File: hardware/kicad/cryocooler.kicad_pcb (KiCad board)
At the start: 4 copper layers, 100 x 62 mm, 330 parts, among them J1 USB_C, J10 RTD PT1000 4-wire, J11 AMP OUT (+ / -), J12 CRYOCOOLER (+ / -), J13 COMPRESSOR RELAY / GND, J14 IMU LSM6DSOX module, J2 12V IN, J3 FAN (4-pin PWM), J4 PUMP (4-pin PWM), J5 ALPHACOOL ES FLOW (3-pin), J6 ALPHACOOL ES NTC 10k, J7 PANEL BUTTON, J8 AMP REM / GND, J9 AMP SIGNAL IN / GND, Q1 IRF4905S, Q10 BSS138, Q11 BSS138, Q12 BSS138, Q2 BSS138, Q3 BSS138, Q4 BSS138, Q5 BSS138, Q6 BSS84, Q7 BSS138, Q8 BSS84, Q9 BSS138, SW1 RESET, SW2 BOOT, SW3 POWER, U1 ESP32-S3-WROOM-2-N32R16V, U10 EMC2303-x-KP, U11 LTC2954CTS8-2, U12 LM4040DBZ-5, U13 CL25N8-G, U14 ADS1220IPW, U15 AP63205WU-7, U16 LD1117S33TR, U17 ISO7741DW, U18 ACS37800KMACTR-030B3-SPI, U2 USBLC6-2SC6, U20 ADP5071AREZ, U21 LT3097ADJC, U23 INA239AIDGSR, U24 74AHCT1G125, U25 SC18IS604PW, U26 74LVC1G125, U3 SG-8002CA-PH 25MHz, U4 AD9833BRMZ, U5 OPA1656ID, U6 AD633JRZ-R7, U7 MCP4921-E/SN, U8 LM4040DBZ-2.5, U9 OPA188ID

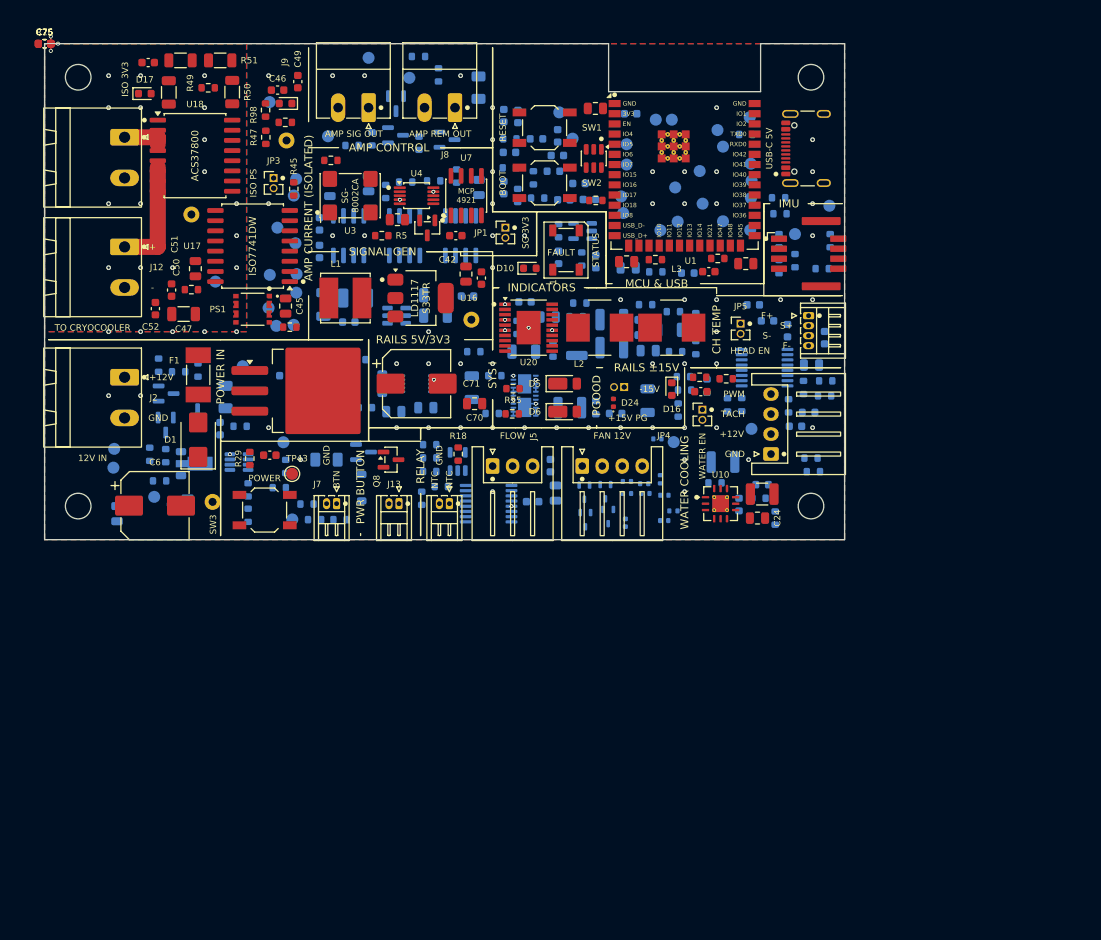
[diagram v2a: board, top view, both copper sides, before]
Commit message: Lay out the board for the Phoenix UCS 145-125 housing
Move to a 120 x 100 mm, 4-layer, blue-mask board for the UCS 145-125-F-CCD
7035 housing: housing mounting holes and restricted corners, ESP32 antenna
over a routed notch, one labelled section per schematic sheet with almost
every part on top. Placed, routed and cleaned up: DRC 0 errors, 0
unconnected, 0 schematic-parity issues; ERC 0; 193/193 datasheet rules.

- AGENTS.md: test points go on the same side as the part they test, close
  to it
- gen_pcb: test points held to their IC's side and within 8 mm; silkscreen
  check measures text by ink and also fails on pads, part outlines, section
  lines and pin-1 dots; titles along or up a border; connector labels and
  ESP32 pin names reserved before the passives; pin-1 dots only where the
  footprint has no mark; footprints carry the schematic's library links and
  fields; mounting holes are board-only H1-H4
- fix_route: generic clean-up (no old-board coordinate edits); removes GND
  vias in keep-outs or on foreign pads, links stranded ground pads, nudges
  squeezed tracks, handles back-side pour islands
- kicad_dru: fix the rule file (an invalid USB-C rule made KiCad ignore it);
  housing-corner and antenna keep-out part rules
- schematic: pad test points excluded from the BOM
- README / fabrication README updated for the new board

Co-Authored-By: Claude Opus 5.5 <noreply@anthropic.com>
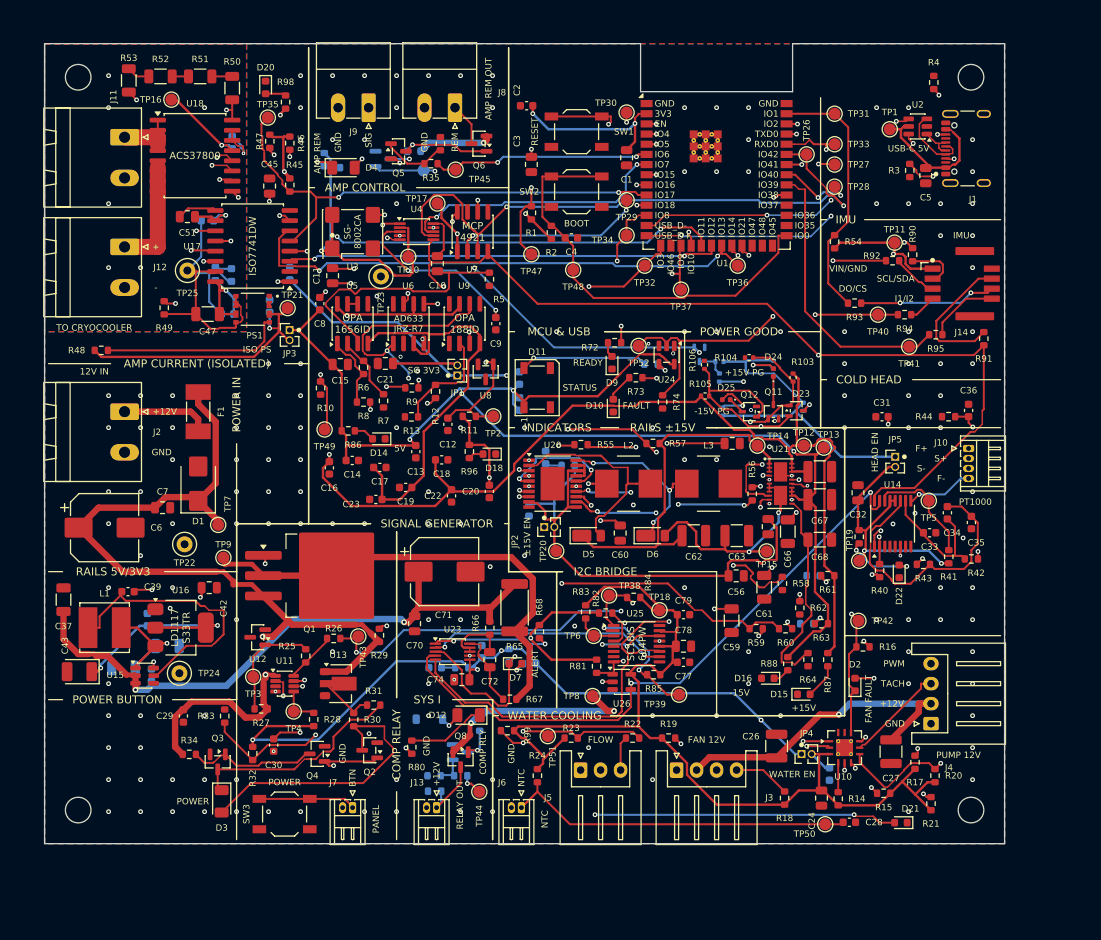
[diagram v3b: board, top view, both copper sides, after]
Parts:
- removed ? (x4): MountingHole_3.2mm_M3, MountingHole_3.2mm_M3
- added H1: MountingHole_3.2mm_M3, MountingHole_3.2mm_M3, F.Cu at (4.20, 4.20)
- added H2: MountingHole_3.2mm_M3, MountingHole_3.2mm_M3, F.Cu at (115.8, 4.20)
- added H3: MountingHole_3.2mm_M3, MountingHole_3.2mm_M3, F.Cu at (4.20, 95.8)
- added H4: MountingHole_3.2mm_M3, MountingHole_3.2mm_M3, F.Cu at (115.8, 95.8)
- C1, C10, C24, C3, C42, C45, C5, C51, C70: footprint C_0805_2012Metric -> Capacitor_SMD:C_0805_2012Metric
- C11, C15, C21, C32, C56, C57, C60, C64, C7, C72, C74, C78: footprint C_0805_2012Metric -> Capacitor_SMD:C_0805_2012Metric; moved to F.Cu
- C12, C13, C14, C16, C17, C18, C19, C2, C20, C22, C23, C30, C31, C33, C34, C35, C36, C39, C77, C79, C9: footprint C_0603_1608Metric -> Capacitor_SMD:C_0603_1608Metric; moved to F.Cu
- C25, C44, C46, C48, C49, C50, C52, C75, C76: footprint C_0603_1608Metric -> Capacitor_SMD:C_0603_1608Metric; moved to B.Cu
- C26: footprint C_1210_3225Metric -> Capacitor_SMD:C_1210_3225Metric
- C27, C62, C63, C65, C67: footprint C_1210_3225Metric -> Capacitor_SMD:C_1210_3225Metric; moved to F.Cu
- C28, C29, C38, C4, C58, C73, C8: footprint C_0603_1608Metric -> Capacitor_SMD:C_0603_1608Metric
- C37, C59, C61, C66, C68: footprint C_1206_3216Metric -> Capacitor_SMD:C_1206_3216Metric; moved to F.Cu
- C40, C41, C47: footprint C_1206_3216Metric -> Capacitor_SMD:C_1206_3216Metric
- C43: footprint CP_EIA-3528-21_Kemet-B -> Capacitor_Tantalum_SMD:CP_EIA-3528-21_Kemet-B; moved to F.Cu
- C6, C71: footprint CP_Elec_8x10 -> Capacitor_SMD:CP_Elec_8x10
- D1: footprint D_SMB -> Diode_SMD:D_SMB
- D10, D16, D19, D20, D8: footprint LED_0603_1608Metric -> LED_SMD:LED_0603_1608Metric
- D11: footprint LED_WS2812B_PLCC4_5.0x5.0mm_P3.2mm -> LED_SMD:LED_WS2812B_PLCC4_5.0x5.0mm_P3.2mm
- D12, D3, D4: footprint LED_1206_3216Metric -> LED_SMD:LED_1206_3216Metric; moved to F.Cu
- D13: footprint D_SOD-123 -> Diode_SMD:D_SOD-123
- D14, D15, D18, D2, D21, D22, D7, D9: footprint LED_0603_1608Metric -> LED_SMD:LED_0603_1608Metric; moved to F.Cu
- D17: footprint LED_0603_1608Metric -> LED_SMD:LED_0603_1608Metric; moved to B.Cu
- D23, Q11, Q12: footprint SOT-323_SC-70 -> Package_TO_SOT_SMD:SOT-323_SC-70; moved to F.Cu
- D24: footprint LED_0402_1005Metric -> LED_SMD:LED_0402_1005Metric
- D25: footprint LED_0402_1005Metric -> LED_SMD:LED_0402_1005Metric; moved to F.Cu
- D5, D6: footprint D_PowerDI-123 -> Diode_SMD:D_PowerDI-123
- F1: footprint Fuse_Littelfuse-NANO2-451_453 -> Fuse:Fuse_Littelfuse-NANO2-451_453
- J1: footprint USB_C_Receptacle_GCT_USB4105-xx-A_16P_TopMnt_Horizontal -> Connector_USB:USB_C_Receptacle_GCT_USB4105-xx-A_16P_TopMnt_Horizontal
- J10: footprint Hirose_DF13-04P-1.25DS_1x04_P1.25mm_Horizontal -> Connector_Hirose:Hirose_DF13-04P-1.25DS_1x04_P1.25mm_Horizontal
- J11, J12, J2: footprint PhoenixContact_MSTBA_2,5_2-G-5,08_1x02_P5.08mm_Horizontal -> Connector_Phoenix_MSTB:PhoenixContact_MSTBA_2,5_2-G-5,08_1x02_P5.08mm_Horizontal
- J13, J6, J7: footprint Hirose_DF13-02P-1.25DS_1x02_P1.25mm_Horizontal -> Connector_Hirose:Hirose_DF13-02P-1.25DS_1x02_P1.25mm_Horizontal
- J14: footprint Molex_Micro-Lock_Plus_505448-0871_2x04_P1.25mm_Horizontal -> cryocooler:Molex_Micro-Lock_Plus_505448-0871_2x04_P1.25mm_Horizontal
- J3, J4: footprint JST_XH_S4B-XH-A_1x04_P2.50mm_Horizontal -> Connector_JST:JST_XH_S4B-XH-A_1x04_P2.50mm_Horizontal
- J5: footprint JST_XH_S3B-XH-A_1x03_P2.50mm_Horizontal -> Connector_JST:JST_XH_S3B-XH-A_1x03_P2.50mm_Horizontal
- J8, J9: footprint PhoenixContact_MC_1,5_2-G-3.81_1x02_P3.81mm_Horizontal -> Connector_Phoenix_MC:PhoenixContact_MC_1,5_2-G-3.81_1x02_P3.81mm_Horizontal
- JP1, JP3, JP4, JP5: footprint PinHeader_1x02_P1.27mm_Vertical -> Connector_PinHeader_1.27mm:PinHeader_1x02_P1.27mm_Vertical
- JP2: footprint PinHeader_1x02_P1.27mm_Vertical -> Connector_PinHeader_1.27mm:PinHeader_1x02_P1.27mm_Vertical; moved to F.Cu
- L1: footprint L_Bourns_SRN6045TA -> Inductor_SMD:L_Bourns_SRN6045TA
- L2, L3: footprint L_Bourns_SRP7050TA -> cryocooler:L_Bourns_SRP7050TA
- PS1: footprint CONV_MIE1W0505BGLVH-3R-Z -> cryocooler:CONV_MIE1W0505BGLVH-3R-Z
- Q1: footprint TO-263-3_TabPin2 -> Package_TO_SOT_SMD:TO-263-3_TabPin2
- Q10: footprint SOT-323_SC-70 -> Package_TO_SOT_SMD:SOT-323_SC-70
- Q2, Q3, Q4, Q5, Q6, U12: footprint SOT-23 -> Package_TO_SOT_SMD:SOT-23; moved to F.Cu
- Q7, Q8, Q9, U8: footprint SOT-23 -> Package_TO_SOT_SMD:SOT-23
- R1, R101, R102, R11, R14, R15, R18, R2, R29, R3, R37, R38, R39, R45, R46, R47, R48, R49, R5, R55, R56, R69, R70, R71, R76, R77, R78, R79, R97, R98: footprint R_0603_1608Metric -> Resistor_SMD:R_0603_1608Metric
- R10, R100, R12, R13, R16, R17, R19, R20, R21, R22, R23, R24, R25, R26, R27, R28, R30, R31, R32, R33, R34, R35, R36, R4, R40, R41, R42, R43, R44, R54, R57, R58, R59, R6, R60, R61, R62, R63, R64, R66, R67, R68, R7, R72, R73, R74, R8, R80, R81, R82, R83, R84, R85, R86, R87, R88, R9, R90, R91, R92, R93, R94, R95, R96, R99: footprint R_0603_1608Metric -> Resistor_SMD:R_0603_1608Metric; moved to F.Cu
- R103, R104, R105, R106: footprint R_0402_1005Metric -> Resistor_SMD:R_0402_1005Metric; moved to F.Cu
- R107, R108, R109, R110, R111: footprint R_0402_1005Metric -> Resistor_SMD:R_0402_1005Metric
- R50, R51, R52, R53: footprint R_1206_3216Metric -> Resistor_SMD:R_1206_3216Metric
- R65: footprint R_2512_6332Metric -> Resistor_SMD:R_2512_6332Metric; moved to F.Cu
- R75, R89: footprint R_0603_1608Metric -> Resistor_SMD:R_0603_1608Metric; moved to B.Cu
- SW1, SW2, SW3: footprint SW_SPST_TL3342 -> Button_Switch_SMD:SW_SPST_TL3342
- TP1, TP10, TP11, TP12, TP13, TP14, TP15, TP16, TP17, TP18, TP19, TP2, TP20, TP21, TP26, TP27, TP28, TP29, TP3, TP30, TP31, TP32, TP33, TP34, TP35, TP36, TP37, TP38, TP39, TP4, TP40, TP41, TP42, TP44, TP45, TP47, TP48, TP49, TP5, TP50, TP51, TP52, TP6, TP7, TP8, TP9: footprint TestPoint_Pad_D1.5mm -> TestPoint:TestPoint_Pad_D1.5mm; moved to F.Cu
- TP22, TP23, TP24, TP25: footprint TestPoint_Loop_D2.50mm_Drill1.0mm -> TestPoint:TestPoint_Loop_D2.50mm_Drill1.0mm; moved to F.Cu
- TP43, TP46: footprint TestPoint_Pad_D1.5mm -> TestPoint:TestPoint_Pad_D1.5mm
- U1: footprint ESP32-S3-WROOM-2 -> RF_Module:ESP32-S3-WROOM-2
- U10: footprint VQFN-12-1EP_4x4mm_P0.8mm_EP2.1x2.1mm_ThermalVias -> Package_DFN_QFN:VQFN-12-1EP_4x4mm_P0.8mm_EP2.1x2.1mm_ThermalVias
- U11: footprint SOT-23-8 -> Package_TO_SOT_SMD:SOT-23-8; moved to F.Cu
- U13: footprint SOT-89-3 -> Package_TO_SOT_SMD:SOT-89-3; moved to F.Cu
- U14, U25: footprint TSSOP-16_4.4x5mm_P0.65mm -> Package_SO:TSSOP-16_4.4x5mm_P0.65mm; moved to F.Cu
- U15: footprint TSOT-23-6 -> Package_TO_SOT_SMD:TSOT-23-6; moved to F.Cu
- U16: footprint SOT-223-3_TabPin2 -> Package_TO_SOT_SMD:SOT-223-3_TabPin2
- U17, U18: footprint SOIC-16W_7.5x10.3mm_P1.27mm -> Package_SO:SOIC-16W_7.5x10.3mm_P1.27mm
- U2: footprint SOT-23-6 -> Package_TO_SOT_SMD:SOT-23-6
- U20: footprint ETSSOP-20-1EP_4.4x6.5mm_P0.65mm_EP3x4.2mm -> Package_SO:ETSSOP-20-1EP_4.4x6.5mm_P0.65mm_EP3x4.2mm
- U21: footprint DFN-22-2EP_6x3mm_P0.5mm_LT3097 -> cryocooler:DFN-22-2EP_6x3mm_P0.5mm_LT3097; moved to F.Cu
- U23: footprint TSSOP-10_3x3mm_P0.5mm -> Package_SO:TSSOP-10_3x3mm_P0.5mm; moved to F.Cu
- U24, U26: footprint SOT-23-5 -> Package_TO_SOT_SMD:SOT-23-5; moved to F.Cu
- U3: footprint Oscillator_SMD_SeikoEpson_SG8002CA-4Pin_7.0x5.0mm -> Oscillator:Oscillator_SMD_SeikoEpson_SG8002CA-4Pin_7.0x5.0mm
- U4: footprint MSOP-10_3x3mm_P0.5mm -> Package_SO:MSOP-10_3x3mm_P0.5mm
- U5, U6, U9: footprint SOIC-8_3.9x4.9mm_P1.27mm -> Package_SO:SOIC-8_3.9x4.9mm_P1.27mm; moved to F.Cu
- U7: footprint SOIC-8_3.9x4.9mm_P1.27mm -> Package_SO:SOIC-8_3.9x4.9mm_P1.27mm
- moved C25 134.0 mm to (98.1, 91.3), turned to -90 degrees
- moved TP19 87.8 mm to (101.8, 64.6)
- moved R75 85.7 mm to (75.8, 40.1), turned to 180 degrees
- moved TP50 83.1 mm to (97.6, 97.6)
- moved C75 74.5 mm to (59.4, 45.0), turned to 90 degrees
- moved C76 72.6 mm to (59.4, 41.8), turned to 90 degrees
- moved TP51 70.4 mm to (62.9, 86.5)
- moved TP39 69.4 mm to (79.3, 81.4)
- moved TP15 69.3 mm to (90.2, 63.5)
- moved TP14 65.9 mm to (89.1, 50.2)
- moved TP8 64.4 mm to (68.5, 81.5)
- moved C38 61.7 mm to (13.4, 79.0), turned to 90 degrees
- moved TP44 61.1 mm to (54.3, 93.5)
- moved C40 60.8 mm to (9.86, 78.0), turned to 180 degrees
- moved TP18 60.5 mm to (76.9, 70.8)
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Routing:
- net +3V3: track 0.00 -> 436.5 mm, vias 0 -> 16
- net +12V: track 0.00 -> 261.5 mm, vias 0 -> 6
- net +5V: track 0.00 -> 248.8 mm, vias 0 -> 6
- net SPI_MOSI: track 0.00 -> 216.3 mm, vias 0 -> 6
- net SPI_SCK: track 0.00 -> 212.9 mm, vias 0 -> 5
- net +15V: track 1.00 -> 162.0 mm, vias 0 -> 2
- net +3V3_COOL: track 0.00 -> 146.8 mm, vias 0 -> 1
- net NTC_ADC: track 0.00 -> 140.2 mm, vias 0 -> 1
- net SPI_MISO: track 0.00 -> 134.6 mm, vias 0 -> 5
- net -15V: track 1.00 -> 133.1 mm, vias 0 -> 2
- net VIN: track 0.00 -> 121.7 mm, vias 0 -> 2
- net PWR_KILL: track 0.00 -> 92.0 mm, vias 0 -> 3
- net FLOW_TACH: track 0.00 -> 88.9 mm, vias 0 -> 2
- net COMP_RELAY_EN: track 0.00 -> 87.8 mm, vias 0 -> 2
- net INA239_CS: track 0.00 -> 74.5 mm, vias 0 -> 3
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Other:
- board size 100 x 62 mm -> 120 x 100 mm
- board text added: "IO0"
- board text added: "IO3"
- board text added: "IO35"
- board text added: "IO46"
- board text added: "IO9"
- board text added: "RELAY OUT"
- board text added: "UCS 145-125 rev 8decd36"
- board text removed: "ADS 1220IPW"
- board text removed: "CH TEMP"
- board text removed: "PGOOD"
- board text removed: "PWR BUTTON"
- board text removed: "RELAY"
- board text removed: "RELAY 12V OUT"
- board text removed: "SIGNAL GEN"
- board text removed: "UCS 125-87 rev 427bca0"
- board text removed: "WATER"
